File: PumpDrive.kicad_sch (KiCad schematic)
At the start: 6 parts, among them Q1 MTB7D0N6RJ3, U4 TLP2348

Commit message: 抜けてたフォトカプラの抵抗を追加
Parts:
- added R7: 560, Resistor_SMD:R_0603_1608Metric_Pad0.98x0.95mm_HandSolder, symbol lib:R_Small
- renumbered R7 to R8, R8 to R9
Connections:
- net PUMP_EN: now also R7.2; no longer U4.3 (K)
- new net: R7.1, U4.3 (K)
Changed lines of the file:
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@@
+	(wire
+		(pts
+			(xy 129.54 110.49) (xy 130.81 110.49)
+		)
+		(stroke
+			(width 0)
+			(type default)
+		)
+	)
 	(wire
 		(pts
@@
 	(wire
 		(pts
-			(xy 128.27 110.49) (xy 130.81 110.49)
+			(xy 121.92 110.49) (xy 124.46 110.49)
 		)
 		(stroke
@@
 	(hierarchical_label "PUMP_EN"
 		(shape input)
-		(at 128.27 110.49 180)
+		(at 121.92 110.49 180)
 		(effects
 			(font
@@
 	)
 	(symbol
+		(lib_id "lib:R_Small")
+		(at 127 110.49 270)
+		(unit 1)
+		(exclude_from_sim no)
+		(in_bom yes)
+		(on_board yes)
+		(dnp no)
+		(fields_autoplaced yes)
+		(property "Reference" "R7"
+			(at 127 105.41 90)
+			(effects
+				(font
+					(size 1.27 1.27)
+				)
+			)
+		)
+		(property "Value" "560"
+			(at 127 107.95 90)
+			(effects
+				(font
+					(size 1.27 1.27)
+				)
+			)
+		)
+		(property "Footprint" "Resistor_SMD:R_0603_1608Metric_Pad0.98x0.95mm_HandSolder"
+			(at 127 110.49 0)
+			(effects
+				(font
+					(size 1.27 1.27)
+				)
+				(hide yes)
+			)
+		)
+		(property "Datasheet" "~"
+			(at 127 110.49 0)
+			(effects
+				(font
+					(size 1.27 1.27)
+				)
+				(hide yes)
+			)
+		)
+		(property "Description" "Resistor, small symbol"
+			(at 127 110.49 0)
+			(effects
+				(font
+					(size 1.27 1.27)
+				)
+				(hide yes)
+			)
+		)
+		(pin "1"
+		)
+		(pin "2"
+		)
+		(instances
+			(project "DRC-PumpDriver2026"
+				(path "/cf42be67-fab3-494c-b2b5-38aff4068810/267e9a6d-86bf-4b07-8799-417cb8de93f0"
+					(reference "R7")
+					(unit 1)
+				)
+				(path "/cf42be67-fab3-494c-b2b5-38aff4068810/6fc723b6-9860-40c7-8b60-dfcef43cdeb1"
+					(reference "R16")
+					(unit 1)
+				)
+				(path "/cf42be67-fab3-494c-b2b5-38aff4068810/78c16eb7-9d88-4e4d-a838-8a7830b1adda"
+					(reference "R13")
+					(unit 1)
+				)
+				(path "/cf42be67-fab3-494c-b2b5-38aff4068810/9f685cf9-fc32-49b8-9759-1a2ea77e2dc8"
+					(reference "R22")
+					(unit 1)
+				)
+				(path "/cf42be67-fab3-494c-b2b5-38aff4068810/f69bd2dd-398c-4f98-a60f-43741652a34b"
+					(reference "R10")
+					(unit 1)
+				)
+				(path "/cf42be67-fab3-494c-b2b5-38aff4068810/f8967fe9-242d-4ee3-b06b-fed4e33255ad"
+					(reference "R19")
+					(unit 1)
+				)
+			)
+		)
+	)
+	(symbol
 		(lib_id "Simulation_SPICE:NMOS")
 		(at 161.29 105.41 0)
@@
 		(dnp no)
 		(fields_autoplaced yes)
-		(property "Reference" "R8"
+		(property "Reference" "R9"
 			(at 166.37 86.3599 0)
 			(effects
@@
 			(project "DRC-PumpDriver2026"
 				(path "/cf42be67-fab3-494c-b2b5-38aff4068810/267e9a6d-86bf-4b07-8799-417cb8de93f0"
-					(reference "R8")
+					(reference "R9")
 					(unit 1)
 				)
 				(path "/cf42be67-fab3-494c-b2b5-38aff4068810/6fc723b6-9860-40c7-8b60-dfcef43cdeb1"
-					(reference "R14")
+					(reference "R18")
 					(unit 1)
 				)
 				(path "/cf42be67-fab3-494c-b2b5-38aff4068810/78c16eb7-9d88-4e4d-a838-8a7830b1adda"
+					(reference "R15")
+					(unit 1)
+				)
+				(path "/cf42be67-fab3-494c-b2b5-38aff4068810/9f685cf9-fc32-49b8-9759-1a2ea77e2dc8"
+					(reference "R24")
+					(unit 1)
+				)
+				(path "/cf42be67-fab3-494c-b2b5-38aff4068810/f69bd2dd-398c-4f98-a60f-43741652a34b"
 					(reference "R12")
 					(unit 1)
 				)
-				(path "/cf42be67-fab3-494c-b2b5-38aff4068810/9f685cf9-fc32-49b8-9759-1a2ea77e2dc8"
-					(reference "R18")
-					(unit 1)
-				)
-				(path "/cf42be67-fab3-494c-b2b5-38aff4068810/f69bd2dd-398c-4f98-a60f-43741652a34b"
-					(reference "R10")
-					(unit 1)
-				)
 				(path "/cf42be67-fab3-494c-b2b5-38aff4068810/f8967fe9-242d-4ee3-b06b-fed4e33255ad"
-					(reference "R16")
+					(reference "R21")
 					(unit 1)
 				)
@@
 		(dnp no)
 		(fields_autoplaced yes)
-		(property "Reference" "R7"
+		(property "Reference" "R8"
 			(at 156.21 110.4899 0)
 			(effects
@@
 			(project "DRC-PumpDriver2026"
 				(path "/cf42be67-fab3-494c-b2b5-38aff4068810/267e9a6d-86bf-4b07-8799-417cb8de93f0"
-					(reference "R7")
+					(reference "R8")
 					(unit 1)
 				)
 				(path "/cf42be67-fab3-494c-b2b5-38aff4068810/6fc723b6-9860-40c7-8b60-dfcef43cdeb1"
-					(reference "R13")
+					(reference "R17")
 					(unit 1)
 				)
 				(path "/cf42be67-fab3-494c-b2b5-38aff4068810/78c16eb7-9d88-4e4d-a838-8a7830b1adda"
+					(reference "R14")
+					(unit 1)
+				)
+				(path "/cf42be67-fab3-494c-b2b5-38aff4068810/9f685cf9-fc32-49b8-9759-1a2ea77e2dc8"
+					(reference "R23")
+					(unit 1)
+				)
+				(path "/cf42be67-fab3-494c-b2b5-38aff4068810/f69bd2dd-398c-4f98-a60f-43741652a34b"
 					(reference "R11")
 					(unit 1)
 				)
-				(path "/cf42be67-fab3-494c-b2b5-38aff4068810/9f685cf9-fc32-49b8-9759-1a2ea77e2dc8"
-					(reference "R17")
-					(unit 1)
-				)
-				(path "/cf42be67-fab3-494c-b2b5-38aff4068810/f69bd2dd-398c-4f98-a60f-43741652a34b"
-					(reference "R9")
-					(unit 1)
-				)
 				(path "/cf42be67-fab3-494c-b2b5-38aff4068810/f8967fe9-242d-4ee3-b06b-fed4e33255ad"
-					(reference "R15")
-					(unit 1)
-				)
+					(reference "R20")
+					(unit 1)
+				)

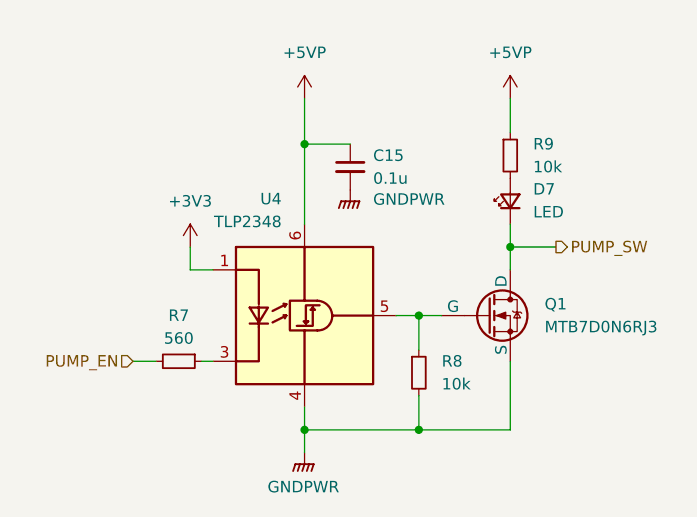
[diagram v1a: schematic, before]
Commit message: DCDCを外して、電源入力に変更、v0.0.2
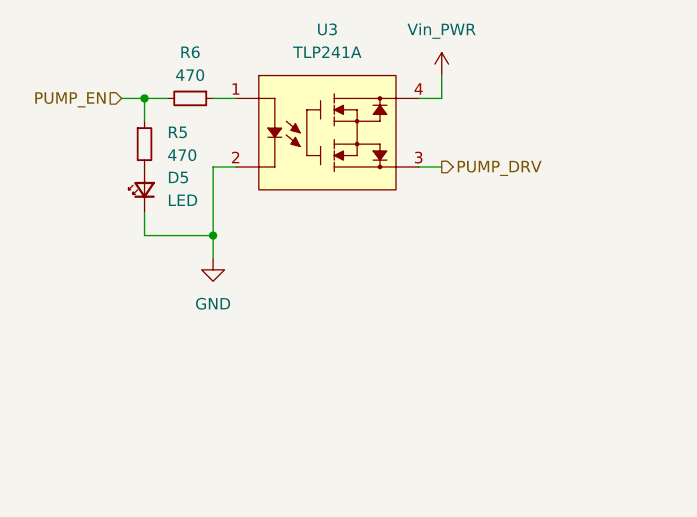
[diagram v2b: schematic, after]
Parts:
- removed C15: 0.1u, Capacitor_SMD:C_0603_1608Metric_Pad1.08x0.95mm_HandSolder, symbol Device:C_Small
- removed Q1: MTB7D0N6RJ3, Package_TO_SOT_SMD:TO-252-2, symbol Simulation_SPICE:NMOS
- removed R8: 10k, Resistor_SMD:R_0603_1608Metric_Pad0.98x0.95mm_HandSolder, symbol lib:R_Small
- removed U4: TLP2348, Package_SO:SO-5-6_4.55x3.7mm_P1.27mm, symbol Isolator:TLP2310
- added U3: TLP241A, lib:DIP4_TOS, symbol lib:TLP241AF
- R5: renamed from R9; value 10k -> 470
- R6: renamed from R7; value 560 -> 470
- renumbered D7 to D5
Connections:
- net +5VP is gone; now on net PUMP_EN: R5.1
- net at R6.1: now also U3.1
- net PUMP_SW renamed GND
- net GND: now also U3.2
- new net PUMP_DRV: U3.3
- new net Vin_PWR: U3.4
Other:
- moved on the sheet: D5, R5, R6

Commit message: STLINK書込みをボックスヘッダへ、USB追加、v0.1.0
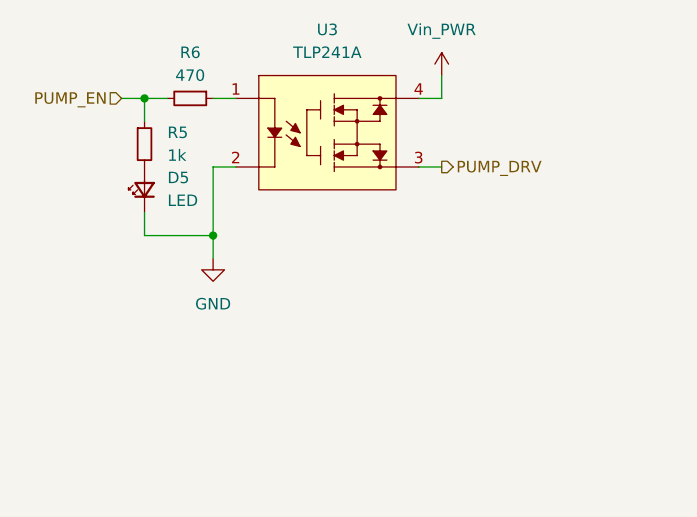
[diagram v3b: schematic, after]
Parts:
- R5: value 470 -> 1k
